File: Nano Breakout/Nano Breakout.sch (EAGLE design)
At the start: 7 parts

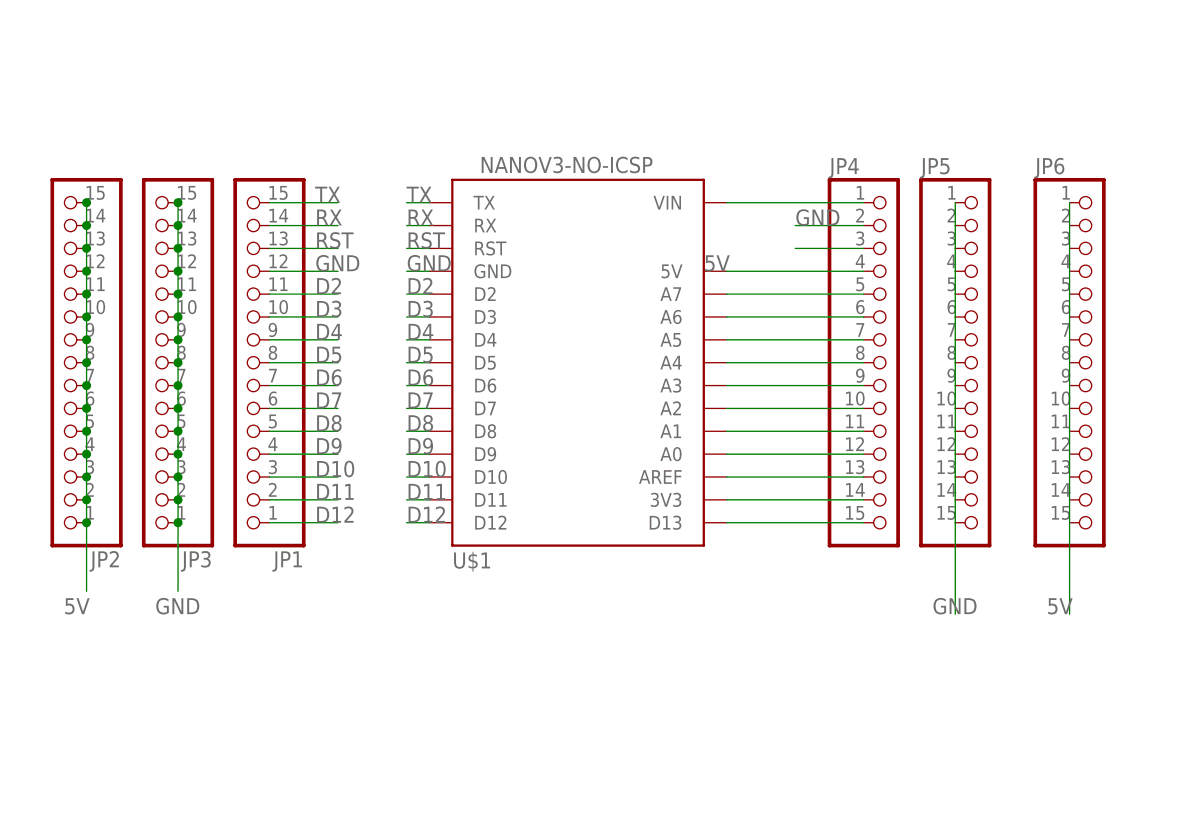
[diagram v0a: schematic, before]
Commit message: remove old dead projects, add esp-01 sensor stuff
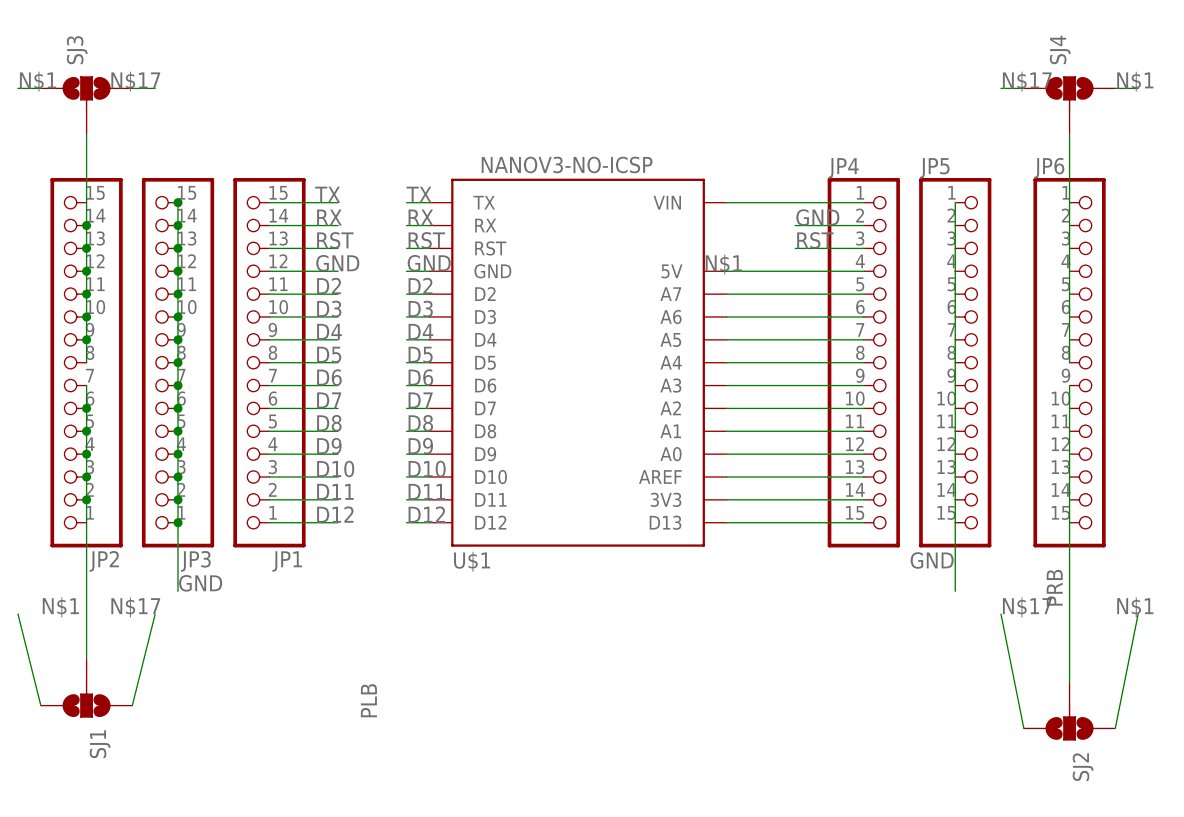
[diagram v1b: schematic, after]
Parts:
- added SJ1, SJ2, SJ3, SJ4: JUMPER-PAD-3-NOFULL_BOX_SILK, SparkFun-Passives:JUMPER-PAD-3-NOFULL_BOX_SILK
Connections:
- removed net 5V: JP2.1, JP2.10, JP2.11, JP2.12, JP2.13, JP2.14, JP2.15, JP2.2, JP2.3, JP2.4, JP2.5, JP2.6, JP2.7, JP2.8, JP2.9, JP4.4, JP6.1, JP6.10, JP6.11, JP6.12, JP6.13, JP6.14, JP6.15, JP6.2, JP6.3, JP6.4, JP6.5, JP6.6, JP6.7, JP6.8, JP6.9, U$1.5V
- new net N$1: JP4.4, SJ1.3, SJ2.1, SJ3.1, SJ4.3, U$1.5V
- new net N$17: JP4.14, SJ1.1, SJ2.3, SJ3.3, SJ4.1, U$1.3V3
- new net N$2: JP2.10, JP2.11, JP2.12, JP2.13, JP2.14, JP2.15, JP2.8, JP2.9, SJ3.2
- new net PLB: JP2.1, JP2.2, JP2.3, JP2.4, JP2.5, JP2.6, JP2.7, SJ1.2
- new net PRB: JP6.10, JP6.11, JP6.12, JP6.13, JP6.14, JP6.15, JP6.9, SJ2.2
- net N$4: now also JP6.1, JP6.2, JP6.3, JP6.4, JP6.5, JP6.6, JP6.7, JP6.8, SJ4.2; no longer JP4.14, U$1.3V3
